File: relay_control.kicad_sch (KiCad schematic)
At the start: 12 parts

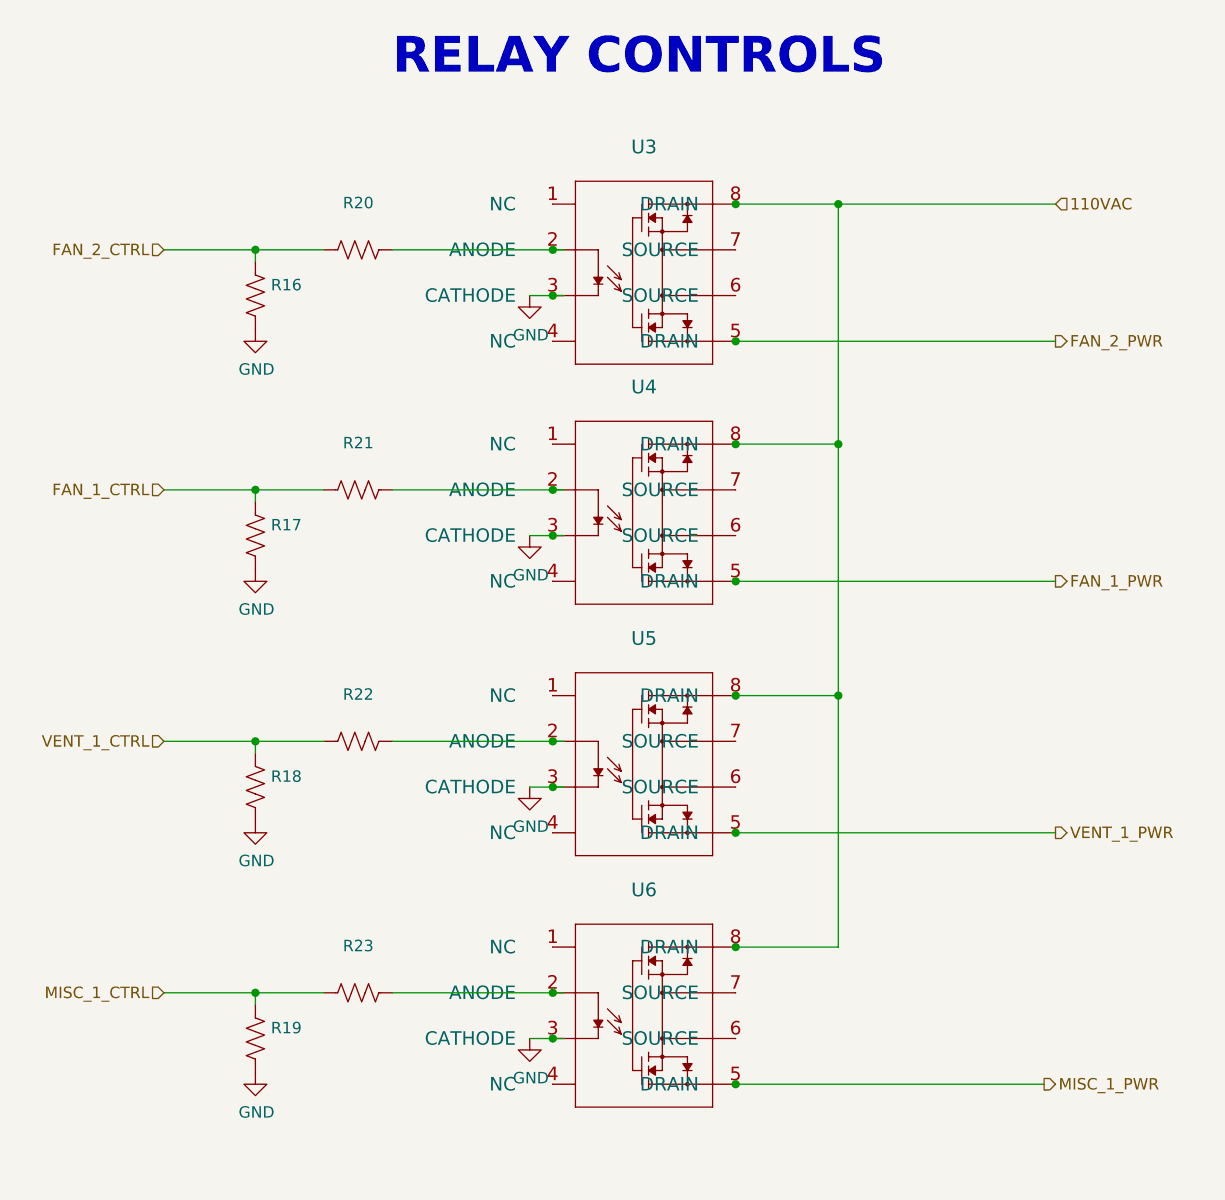
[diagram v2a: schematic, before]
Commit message: Finished initial layout.  Zero DRC errors/warnings.
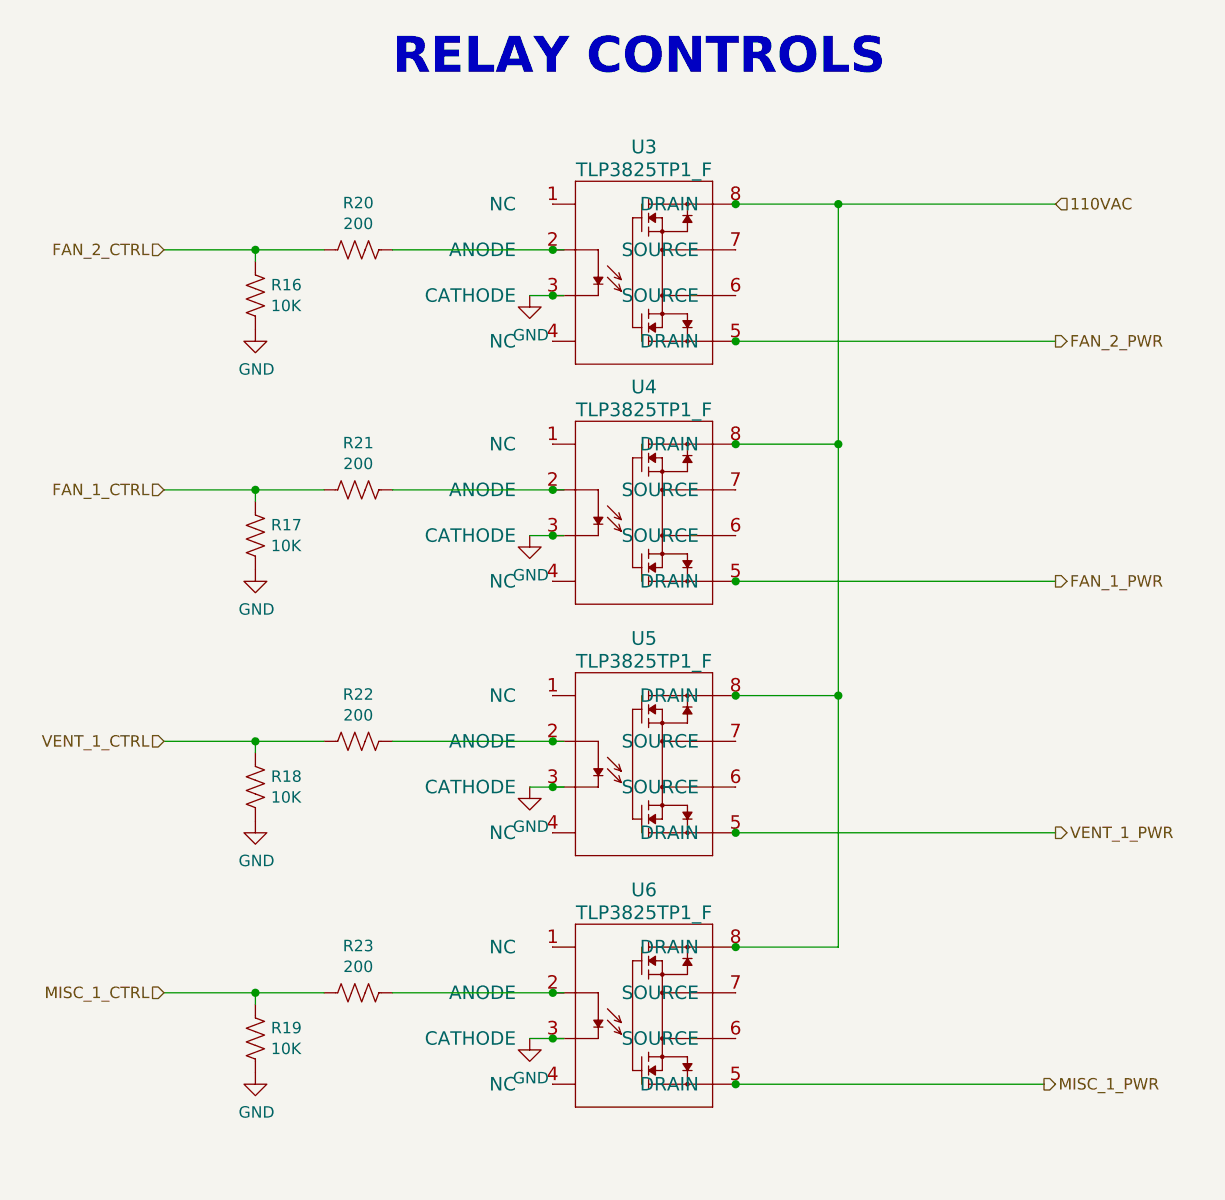
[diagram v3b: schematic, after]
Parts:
- R16, R17, R18, R19: value (none) -> 10K; footprint (none) -> Resistor_SMD:R_0805_2012Metric
- R20, R21, R22, R23: value (none) -> 200; footprint (none) -> Resistor_SMD:R_0805_2012Metric
- U3, U4, U5, U6: value (none) -> TLP3825TP1_F; footprint (none) -> Package_DIP:DIP-8_W7.62mm
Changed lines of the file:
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@@
     (in_bom yes) (on_board yes)
     (property "Reference" "R21" (id 0) (at 120.65 69.723 90))
-    (property "Value" "" (id 1) (at 120.65 72.0344 90))
-    (property "Footprint" "" (id 2) (at 120.396 75.946 90)
+    (property "Value" "200" (id 1) (at 120.65 72.0344 90))
+    (property "Footprint" "Resistor_SMD:R_0805_2012Metric" (id 2) (at 120.396 75.946 90)
       (effects (font (size 1.27 1.27)) hide)
     )
@@
       (effects (font (size 1.27 1.27)) (justify left))
     )
-    (property "Value" "" (id 1) (at 110.9472 81.153 0)
-      (effects (font (size 1.27 1.27)) (justify left))
-    )
-    (property "Footprint" "" (id 2) (at 110.236 80.264 90)
+    (property "Value" "10K" (id 1) (at 110.9472 81.153 0)
+      (effects (font (size 1.27 1.27)) (justify left))
+    )
+    (property "Footprint" "Resistor_SMD:R_0805_2012Metric" (id 2) (at 110.236 80.264 90)
       (effects (font (size 1.27 1.27)) hide)
     )
@@
     (in_bom yes) (on_board yes)
     (property "Reference" "R20" (id 0) (at 120.65 43.053 90))
-    (property "Value" "" (id 1) (at 120.65 45.3644 90))
-    (property "Footprint" "" (id 2) (at 120.396 49.276 90)
+    (property "Value" "200" (id 1) (at 120.65 45.3644 90))
+    (property "Footprint" "Resistor_SMD:R_0805_2012Metric" (id 2) (at 120.396 49.276 90)
       (effects (font (size 1.27 1.27)) hide)
     )
@@
       (effects (font (size 1.27 1.27)) (justify left))
     )
-    (property "Value" "" (id 1) (at 110.9472 54.483 0)
-      (effects (font (size 1.27 1.27)) (justify left))
-    )
-    (property "Footprint" "" (id 2) (at 110.236 53.594 90)
+    (property "Value" "10K" (id 1) (at 110.9472 54.483 0)
+      (effects (font (size 1.27 1.27)) (justify left))
+    )
+    (property "Footprint" "Resistor_SMD:R_0805_2012Metric" (id 2) (at 110.236 53.594 90)
       (effects (font (size 1.27 1.27)) hide)
     )
@@
     (in_bom yes) (on_board yes)
     (property "Reference" "R22" (id 0) (at 120.65 97.663 90))
-    (property "Value" "" (id 1) (at 120.65 99.9744 90))
-    (property "Footprint" "" (id 2) (at 120.396 103.886 90)
+    (property "Value" "200" (id 1) (at 120.65 99.9744 90))
+    (property "Footprint" "Resistor_SMD:R_0805_2012Metric" (id 2) (at 120.396 103.886 90)
       (effects (font (size 1.27 1.27)) hide)
     )
@@
       (effects (font (size 1.27 1.27)) (justify left))
     )
-    (property "Value" "" (id 1) (at 110.9472 109.093 0)
-      (effects (font (size 1.27 1.27)) (justify left))
-    )
-    (property "Footprint" "" (id 2) (at 110.236 108.204 90)
+    (property "Value" "10K" (id 1) (at 110.9472 109.093 0)
+      (effects (font (size 1.27 1.27)) (justify left))
+    )
+    (property "Footprint" "Resistor_SMD:R_0805_2012Metric" (id 2) (at 110.236 108.204 90)
       (effects (font (size 1.27 1.27)) hide)
     )
@@
     (in_bom yes) (on_board yes)
     (property "Reference" "R23" (id 0) (at 120.65 125.603 90))
-    (property "Value" "" (id 1) (at 120.65 127.9144 90))
-    (property "Footprint" "" (id 2) (at 120.396 131.826 90)
+    (property "Value" "200" (id 1) (at 120.65 127.9144 90))
+    (property "Footprint" "Resistor_SMD:R_0805_2012Metric" (id 2) (at 120.396 131.826 90)
       (effects (font (size 1.27 1.27)) hide)
     )
@@
       (effects (font (size 1.27 1.27)) (justify left))
     )
-    (property "Value" "" (id 1) (at 110.9472 137.033 0)
-      (effects (font (size 1.27 1.27)) (justify left))
-    )
-    (property "Footprint" "" (id 2) (at 110.236 136.144 90)
+    (property "Value" "10K" (id 1) (at 110.9472 137.033 0)
+      (effects (font (size 1.27 1.27)) (justify left))
+    )
+    (property "Footprint" "Resistor_SMD:R_0805_2012Metric" (id 2) (at 110.236 136.144 90)
       (effects (font (size 1.27 1.27)) hide)
     )
@@
       (effects (font (size 1.524 1.524)))
     )
-    (property "Value" "" (id 1) (at 152.4 66.04 0)
-      (effects (font (size 1.524 1.524)))
-    )
-    (property "Footprint" "" (id 2) (at 144.78 67.31 0)
+    (property "Value" "TLP3825TP1_F" (id 1) (at 152.4 66.04 0)
+      (effects (font (size 1.524 1.524)))
+    )
+    (property "Footprint" "Package_DIP:DIP-8_W7.62mm" (id 2) (at 144.78 67.31 0)
       (effects (font (size 1.524 1.524)) hide)
     )
@@
       (effects (font (size 1.524 1.524)))
     )
-    (property "Value" "" (id 1) (at 152.4 39.37 0)
-      (effects (font (size 1.524 1.524)))
-    )
-    (property "Footprint" "" (id 2) (at 144.78 40.64 0)
+    (property "Value" "TLP3825TP1_F" (id 1) (at 152.4 39.37 0)
+      (effects (font (size 1.524 1.524)))
+    )
+    (property "Footprint" "Package_DIP:DIP-8_W7.62mm" (id 2) (at 144.78 40.64 0)
       (effects (font (size 1.524 1.524)) hide)
     )
@@
       (effects (font (size 1.524 1.524)))
     )
-    (property "Value" "" (id 1) (at 152.4 121.92 0)
-      (effects (font (size 1.524 1.524)))
-    )
-    (property "Footprint" "" (id 2) (at 144.78 123.19 0)
+    (property "Value" "TLP3825TP1_F" (id 1) (at 152.4 121.92 0)
+      (effects (font (size 1.524 1.524)))
+    )
+    (property "Footprint" "Package_DIP:DIP-8_W7.62mm" (id 2) (at 144.78 123.19 0)
       (effects (font (size 1.524 1.524)) hide)
     )
@@
       (effects (font (size 1.524 1.524)))
     )
-    (property "Value" "" (id 1) (at 152.4 93.98 0)
-      (effects (font (size 1.524 1.524)))
-    )
-    (property "Footprint" "" (id 2) (at 144.78 95.25 0)
-      (effects (font (size 1.524 1.524)) hide)
-    )
+    (property "Value" "TLP3825TP1_F" (id 1) (at 152.4 93.98 0)
+      (effects (font (size 1.524 1.524)))
+    )
+    (property "Footprint" "Package_DIP:DIP-8_W7.62mm" (id 2) (at 144.78 95.25 0)
+      (effects (font (size 1.524 1.524)) hide)
+    )

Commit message: Replaced relays with smd versions.
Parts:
- R16, R17, R18, R19: value 10K -> (none); footprint Resistor_SMD:R_0805_2012Metric -> (none)
- R20, R21, R22, R23: value 200 -> (none); footprint Resistor_SMD:R_0805_2012Metric -> (none)
- U3, U4, U5, U6: value TLP3825TP1_F -> (none); footprint Package_DIP:DIP-8_W7.62mm -> (none)
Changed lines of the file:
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@@
     (in_bom yes) (on_board yes)
     (property "Reference" "R21" (id 0) (at 120.65 69.723 90))
-    (property "Value" "200" (id 1) (at 120.65 72.0344 90))
-    (property "Footprint" "Resistor_SMD:R_0805_2012Metric" (id 2) (at 120.396 75.946 90)
+    (property "Value" "" (id 1) (at 120.65 72.0344 90))
+    (property "Footprint" "" (id 2) (at 120.396 75.946 90)
       (effects (font (size 1.27 1.27)) hide)
     )
@@
       (effects (font (size 1.27 1.27)) (justify left))
     )
-    (property "Value" "10K" (id 1) (at 110.9472 81.153 0)
-      (effects (font (size 1.27 1.27)) (justify left))
-    )
-    (property "Footprint" "Resistor_SMD:R_0805_2012Metric" (id 2) (at 110.236 80.264 90)
+    (property "Value" "" (id 1) (at 110.9472 81.153 0)
+      (effects (font (size 1.27 1.27)) (justify left))
+    )
+    (property "Footprint" "" (id 2) (at 110.236 80.264 90)
       (effects (font (size 1.27 1.27)) hide)
     )
@@
     (in_bom yes) (on_board yes)
     (property "Reference" "R20" (id 0) (at 120.65 43.053 90))
-    (property "Value" "200" (id 1) (at 120.65 45.3644 90))
-    (property "Footprint" "Resistor_SMD:R_0805_2012Metric" (id 2) (at 120.396 49.276 90)
+    (property "Value" "" (id 1) (at 120.65 45.3644 90))
+    (property "Footprint" "" (id 2) (at 120.396 49.276 90)
       (effects (font (size 1.27 1.27)) hide)
     )
@@
       (effects (font (size 1.27 1.27)) (justify left))
     )
-    (property "Value" "10K" (id 1) (at 110.9472 54.483 0)
-      (effects (font (size 1.27 1.27)) (justify left))
-    )
-    (property "Footprint" "Resistor_SMD:R_0805_2012Metric" (id 2) (at 110.236 53.594 90)
+    (property "Value" "" (id 1) (at 110.9472 54.483 0)
+      (effects (font (size 1.27 1.27)) (justify left))
+    )
+    (property "Footprint" "" (id 2) (at 110.236 53.594 90)
       (effects (font (size 1.27 1.27)) hide)
     )
@@
     (in_bom yes) (on_board yes)
     (property "Reference" "R22" (id 0) (at 120.65 97.663 90))
-    (property "Value" "200" (id 1) (at 120.65 99.9744 90))
-    (property "Footprint" "Resistor_SMD:R_0805_2012Metric" (id 2) (at 120.396 103.886 90)
+    (property "Value" "" (id 1) (at 120.65 99.9744 90))
+    (property "Footprint" "" (id 2) (at 120.396 103.886 90)
       (effects (font (size 1.27 1.27)) hide)
     )
@@
       (effects (font (size 1.27 1.27)) (justify left))
     )
-    (property "Value" "10K" (id 1) (at 110.9472 109.093 0)
-      (effects (font (size 1.27 1.27)) (justify left))
-    )
-    (property "Footprint" "Resistor_SMD:R_0805_2012Metric" (id 2) (at 110.236 108.204 90)
+    (property "Value" "" (id 1) (at 110.9472 109.093 0)
+      (effects (font (size 1.27 1.27)) (justify left))
+    )
+    (property "Footprint" "" (id 2) (at 110.236 108.204 90)
       (effects (font (size 1.27 1.27)) hide)
     )
@@
     (in_bom yes) (on_board yes)
     (property "Reference" "R23" (id 0) (at 120.65 125.603 90))
-    (property "Value" "200" (id 1) (at 120.65 127.9144 90))
-    (property "Footprint" "Resistor_SMD:R_0805_2012Metric" (id 2) (at 120.396 131.826 90)
+    (property "Value" "" (id 1) (at 120.65 127.9144 90))
+    (property "Footprint" "" (id 2) (at 120.396 131.826 90)
       (effects (font (size 1.27 1.27)) hide)
     )
@@
       (effects (font (size 1.27 1.27)) (justify left))
     )
-    (property "Value" "10K" (id 1) (at 110.9472 137.033 0)
-      (effects (font (size 1.27 1.27)) (justify left))
-    )
-    (property "Footprint" "Resistor_SMD:R_0805_2012Metric" (id 2) (at 110.236 136.144 90)
+    (property "Value" "" (id 1) (at 110.9472 137.033 0)
+      (effects (font (size 1.27 1.27)) (justify left))
+    )
+    (property "Footprint" "" (id 2) (at 110.236 136.144 90)
       (effects (font (size 1.27 1.27)) hide)
     )
@@
       (effects (font (size 1.524 1.524)))
     )
-    (property "Value" "TLP3825TP1_F" (id 1) (at 152.4 66.04 0)
-      (effects (font (size 1.524 1.524)))
-    )
-    (property "Footprint" "Package_DIP:DIP-8_W7.62mm" (id 2) (at 144.78 67.31 0)
+    (property "Value" "" (id 1) (at 152.4 66.04 0)
+      (effects (font (size 1.524 1.524)))
+    )
+    (property "Footprint" "" (id 2) (at 144.78 67.31 0)
       (effects (font (size 1.524 1.524)) hide)
     )
@@
       (effects (font (size 1.524 1.524)))
     )
-    (property "Value" "TLP3825TP1_F" (id 1) (at 152.4 39.37 0)
-      (effects (font (size 1.524 1.524)))
-    )
-    (property "Footprint" "Package_DIP:DIP-8_W7.62mm" (id 2) (at 144.78 40.64 0)
+    (property "Value" "" (id 1) (at 152.4 39.37 0)
+      (effects (font (size 1.524 1.524)))
+    )
+    (property "Footprint" "" (id 2) (at 144.78 40.64 0)
       (effects (font (size 1.524 1.524)) hide)
     )
@@
       (effects (font (size 1.524 1.524)))
     )
-    (property "Value" "TLP3825TP1_F" (id 1) (at 152.4 121.92 0)
-      (effects (font (size 1.524 1.524)))
-    )
-    (property "Footprint" "Package_DIP:DIP-8_W7.62mm" (id 2) (at 144.78 123.19 0)
+    (property "Value" "" (id 1) (at 152.4 121.92 0)
+      (effects (font (size 1.524 1.524)))
+    )
+    (property "Footprint" "" (id 2) (at 144.78 123.19 0)
       (effects (font (size 1.524 1.524)) hide)
     )
@@
       (effects (font (size 1.524 1.524)))
     )
-    (property "Value" "TLP3825TP1_F" (id 1) (at 152.4 93.98 0)
-      (effects (font (size 1.524 1.524)))
-    )
-    (property "Footprint" "Package_DIP:DIP-8_W7.62mm" (id 2) (at 144.78 95.25 0)
-      (effects (font (size 1.524 1.524)) hide)
-    )
+    (property "Value" "" (id 1) (at 152.4 93.98 0)
+      (effects (font (size 1.524 1.524)))
+    )
+    (property "Footprint" "" (id 2) (at 144.78 95.25 0)
+      (effects (font (size 1.524 1.524)) hide)
+    )
